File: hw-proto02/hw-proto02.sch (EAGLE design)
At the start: 21 parts, among them IC1 VN5E160MSTR-E, IC3 MCP2562T, IC5 IR4427S, J1 000, J2 000, Q1 SQJ147ELP-T1_GE3, Q2 SQJ147ELP-T1_GE3

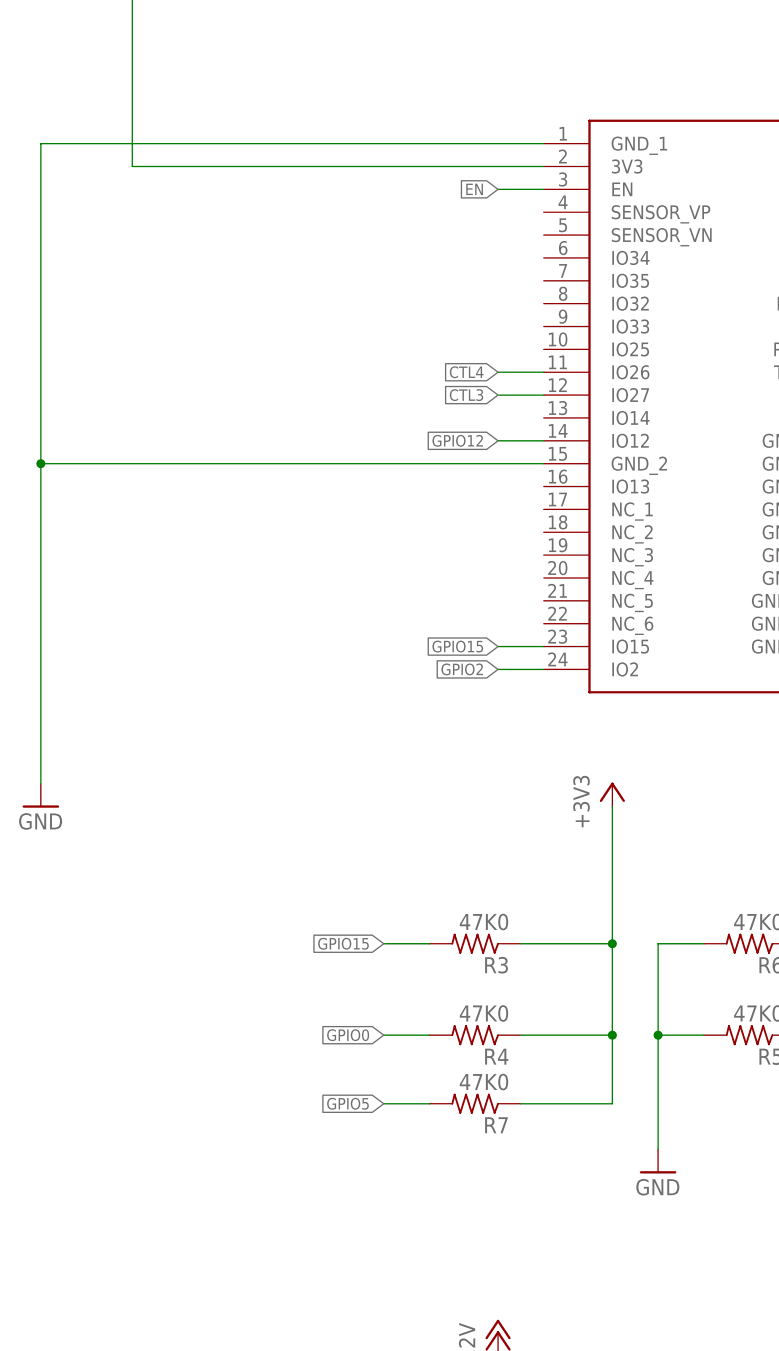
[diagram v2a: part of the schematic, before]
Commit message: power layout adjustment, added passives
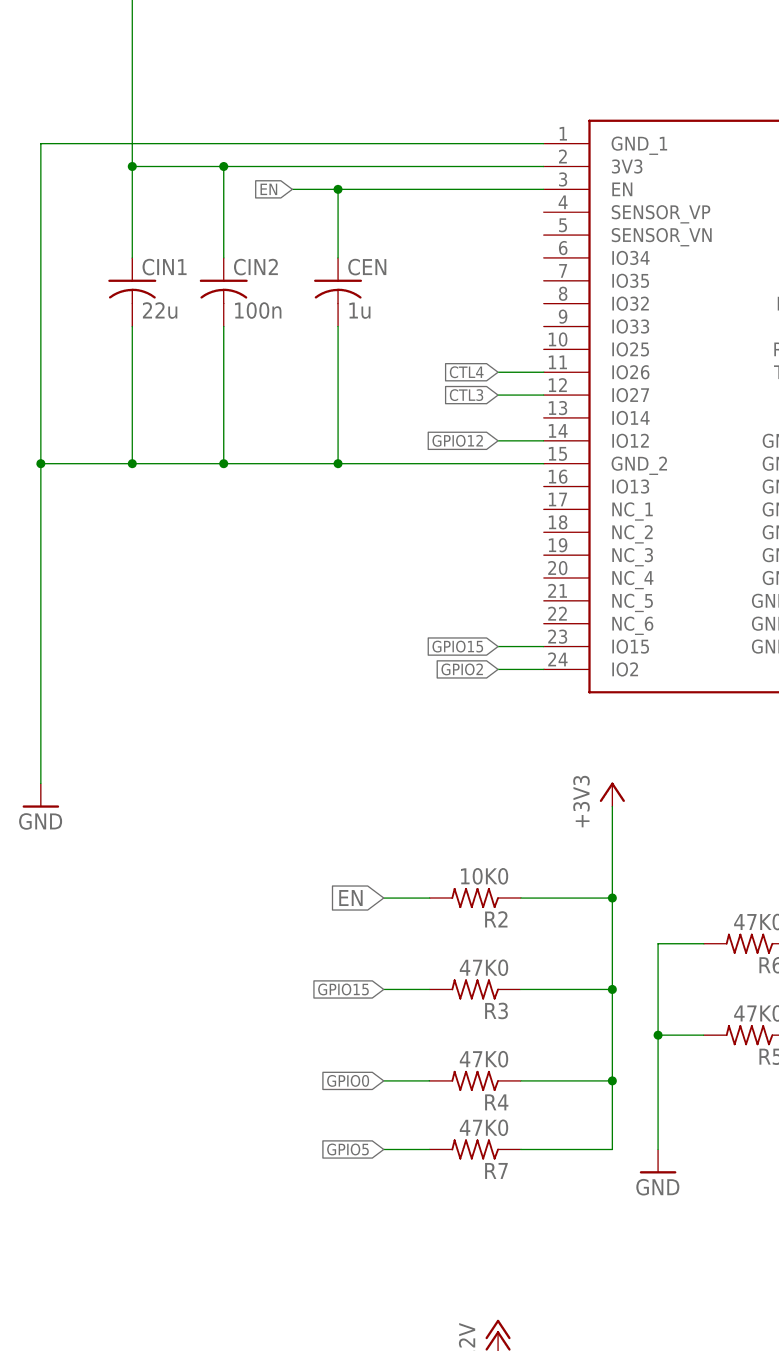
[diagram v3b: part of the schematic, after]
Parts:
- added CEN: 1u, rcl:C-USC0603K
- added CIN1: 22u, rcl:C-USC0805K
- added CIN2: 100n, rcl:C-USC0603K
- added R2: 10K0, rcl:R-US_R0603
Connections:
- net +3V3: now also CIN1.1, CIN2.1, R2.1
- net EN: now also CEN.1, R2.2
- net GND: now also CEN.2, CIN1.2, CIN2.2
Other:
- moved on the sheet: R3, R4, R7
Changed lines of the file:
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@@
 <part name="Q1" library="transistor-vishay-pchan-pso8" deviceset="SQJ147ELP-T1_GE3" device=""/>
 <part name="Q2" library="transistor-vishay-pchan-pso8" deviceset="SQJ147ELP-T1_GE3" device=""/>
+<part name="R2" library="rcl" deviceset="R-US_" device="R0603" value="10K0"/>
+<part name="CIN1" library="rcl" deviceset="C-US" device="C0805K" value="22u"/>
+<part name="CIN2" library="rcl" deviceset="C-US" device="C0603K" value="100n"/>
+<part name="CEN" library="rcl" deviceset="C-US" device="C0603K" value="1u"/>
 </parts>
 <sheets>
@@
 <instance part="C1" gate="G$1" x="63.5" y="213.36"/>
 <instance part="C2" gate="G$1" x="134.62" y="203.2"/>
-<instance part="R3" gate="G$1" x="-12.7" y="137.16" rot="R180"/>
-<instance part="R4" gate="G$1" x="-12.7" y="127" rot="R180"/>
+<instance part="R3" gate="G$1" x="-12.7" y="132.08" rot="R180"/>
+<instance part="R4" gate="G$1" x="-12.7" y="121.92" rot="R180"/>
 <instance part="R5" gate="G$1" x="17.78" y="127" rot="R180"/>
 <instance part="+3V3" gate="G$1" x="2.54" y="154.94"/>
 <instance part="GND10" gate="1" x="7.62" y="111.76"/>
 <instance part="R6" gate="G$1" x="17.78" y="137.16" rot="R180"/>
-<instance part="R7" gate="G$1" x="-12.7" y="119.38" rot="R180"/>
+<instance part="R7" gate="G$1" x="-12.7" y="114.3" rot="R180"/>
 <instance part="PROG" gate="G$1" x="220.98" y="93.98"/>
 <instance part="GND11" gate="1" x="200.66" y="73.66"/>
 <instance part="Q1" gate="G$1" x="12.7" y="81.28"/>
 <instance part="Q2" gate="G$1" x="50.8" y="81.28"/>
+<instance part="R2" gate="G$1" x="-12.7" y="142.24" rot="R180"/>
+<instance part="CIN1" gate="G$1" x="-50.8" y="210.82"/>
+<instance part="CIN2" gate="G$1" x="-40.64" y="210.82"/>
+<instance part="CEN" gate="G$1" x="-27.94" y="210.82"/>
 </instances>
 <busses>
@@
 <pinref part="MCU" gate="G$1" pin="GND_2"/>
 <wire x1="-60.96" y1="190.5" x2="-60.96" y2="154.94" width="0.1524" layer="91"/>
-<wire x1="-5.08" y1="190.5" x2="-60.96" y2="190.5" width="0.1524" layer="91"/>
+<wire x1="-5.08" y1="190.5" x2="-27.94" y2="190.5" width="0.1524" layer="91"/>
 <junction x="-60.96" y="190.5"/>
+<pinref part="CIN2" gate="G$1" pin="2"/>
+<wire x1="-27.94" y1="190.5" x2="-40.64" y2="190.5" width="0.1524" layer="91"/>
+<wire x1="-40.64" y1="190.5" x2="-50.8" y2="190.5" width="0.1524" layer="91"/>
+<wire x1="-50.8" y1="190.5" x2="-60.96" y2="190.5" width="0.1524" layer="91"/>
+<wire x1="-40.64" y1="205.74" x2="-40.64" y2="190.5" width="0.1524" layer="91"/>
+<junction x="-40.64" y="190.5"/>
+<pinref part="CIN1" gate="G$1" pin="2"/>
+<wire x1="-50.8" y1="205.74" x2="-50.8" y2="190.5" width="0.1524" layer="91"/>
+<junction x="-50.8" y="190.5"/>
+<pinref part="CEN" gate="G$1" pin="2"/>
+<wire x1="-27.94" y1="205.74" x2="-27.94" y2="190.5" width="0.1524" layer="91"/>
+<junction x="-27.94" y="190.5"/>
 </segment>
 <segment>
@@
 <pinref part="MCU" gate="G$1" pin="3V3"/>
 <pinref part="+3V2" gate="G$1" pin="+3V3"/>
-<wire x1="-5.08" y1="223.52" x2="-50.8" y2="223.52" width="0.1524" layer="91"/>
+<wire x1="-5.08" y1="223.52" x2="-40.64" y2="223.52" width="0.1524" layer="91"/>
+<wire x1="-40.64" y1="223.52" x2="-50.8" y2="223.52" width="0.1524" layer="91"/>
 <wire x1="-50.8" y1="223.52" x2="-50.8" y2="254" width="0.1524" layer="91"/>
+<pinref part="CIN1" gate="G$1" pin="1"/>
+<wire x1="-50.8" y1="213.36" x2="-50.8" y2="223.52" width="0.1524" layer="91"/>
+<junction x="-50.8" y="223.52"/>
+<pinref part="CIN2" gate="G$1" pin="1"/>
+<wire x1="-40.64" y1="213.36" x2="-40.64" y2="223.52" width="0.1524" layer="91"/>
+<junction x="-40.64" y="223.52"/>
 </segment>
 <segment>
@@
 <pinref part="R4" gate="G$1" pin="1"/>
 <pinref part="+3V3" gate="G$1" pin="+3V3"/>
-<wire x1="-7.62" y1="127" x2="2.54" y2="127" width="0.1524" layer="91"/>
-<wire x1="2.54" y1="127" x2="2.54" y2="137.16" width="0.1524" layer="91"/>
+<wire x1="-7.62" y1="121.92" x2="2.54" y2="121.92" width="0.1524" layer="91"/>
+<wire x1="2.54" y1="121.92" x2="2.54" y2="132.08" width="0.1524" layer="91"/>
 <pinref part="R3" gate="G$1" pin="1"/>
-<wire x1="2.54" y1="137.16" x2="2.54" y2="152.4" width="0.1524" layer="91"/>
-<wire x1="-7.62" y1="137.16" x2="2.54" y2="137.16" width="0.1524" layer="91"/>
-<junction x="2.54" y="137.16"/>
+<wire x1="2.54" y1="132.08" x2="2.54" y2="142.24" width="0.1524" layer="91"/>
+<wire x1="2.54" y1="142.24" x2="2.54" y2="152.4" width="0.1524" layer="91"/>
+<wire x1="-7.62" y1="132.08" x2="2.54" y2="132.08" width="0.1524" layer="91"/>
+<junction x="2.54" y="132.08"/>
 <pinref part="R7" gate="G$1" pin="1"/>
-<wire x1="-7.62" y1="119.38" x2="2.54" y2="119.38" width="0.1524" layer="91"/>
-<wire x1="2.54" y1="119.38" x2="2.54" y2="127" width="0.1524" layer="91"/>
-<junction x="2.54" y="127"/>
+<wire x1="-7.62" y1="114.3" x2="2.54" y2="114.3" width="0.1524" layer="91"/>
+<wire x1="2.54" y1="114.3" x2="2.54" y2="121.92" width="0.1524" layer="91"/>
+<junction x="2.54" y="121.92"/>
+<pinref part="R2" gate="G$1" pin="1"/>
+<wire x1="-7.62" y1="142.24" x2="2.54" y2="142.24" width="0.1524" layer="91"/>
+<junction x="2.54" y="142.24"/>
 </segment>
 </net>
@@
 <segment>
 <pinref part="R3" gate="G$1" pin="2"/>
-<wire x1="-22.86" y1="137.16" x2="-17.78" y2="137.16" width="0.1524" layer="91"/>
-<label x="-22.86" y="137.16" size="1.27" layer="95" rot="R180" xref="yes"/>
+<wire x1="-22.86" y1="132.08" x2="-17.78" y2="132.08" width="0.1524" layer="91"/>
+<label x="-22.86" y="132.08" size="1.27" layer="95" rot="R180" xref="yes"/>
 </segment>
 </net>
@@
 <segment>
 <pinref part="R4" gate="G$1" pin="2"/>
-<wire x1="-22.86" y1="127" x2="-17.78" y2="127" width="0.1524" layer="91"/>
-<label x="-22.86" y="127" size="1.27" layer="95" rot="R180" xref="yes"/>
+<wire x1="-22.86" y1="121.92" x2="-17.78" y2="121.92" width="0.1524" layer="91"/>
+<label x="-22.86" y="121.92" size="1.27" layer="95" rot="R180" xref="yes"/>
 </segment>
 <segment>
@@
 <segment>
 <pinref part="R7" gate="G$1" pin="2"/>
-<wire x1="-22.86" y1="119.38" x2="-17.78" y2="119.38" width="0.1524" layer="91"/>
-<label x="-22.86" y="119.38" size="1.27" layer="95" rot="R180" xref="yes"/>
+<wire x1="-22.86" y1="114.3" x2="-17.78" y2="114.3" width="0.1524" layer="91"/>
+<label x="-22.86" y="114.3" size="1.27" layer="95" rot="R180" xref="yes"/>
 </segment>
 <segment>
@@
 <segment>
 <pinref part="MCU" gate="G$1" pin="EN"/>
-<wire x1="-10.16" y1="220.98" x2="-5.08" y2="220.98" width="0.1524" layer="91"/>
-<label x="-10.16" y="220.98" size="1.27" layer="95" rot="R180" xref="yes"/>
+<wire x1="-33.02" y1="220.98" x2="-27.94" y2="220.98" width="0.1524" layer="91"/>
+<label x="-33.02" y="220.98" size="1.27" layer="95" rot="R180" xref="yes"/>
+<pinref part="CEN" gate="G$1" pin="1"/>
+<wire x1="-27.94" y1="220.98" x2="-5.08" y2="220.98" width="0.1524" layer="91"/>
+<wire x1="-27.94" y1="213.36" x2="-27.94" y2="220.98" width="0.1524" layer="91"/>
+<junction x="-27.94" y="220.98"/>
 </segment>
 <segment>
@@
 <label x="208.28" y="93.98" size="1.27" layer="95" rot="R180" xref="yes"/>
 </segment>
-</net>
+<segment>
+<pinref part="R2" gate="G$1" pin="2"/>
+<wire x1="-22.86" y1="142.24" x2="-17.78" y2="142.24" width="0.1524" layer="91"/>
+<label x="-22.86" y="142.24" size="1.778" layer="95" rot="R180" xref="yes"/>
+</segment>
+</net>
